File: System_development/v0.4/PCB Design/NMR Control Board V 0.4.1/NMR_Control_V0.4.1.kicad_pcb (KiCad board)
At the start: 2 copper layers, 139.7 x 88.9 mm, 57 parts

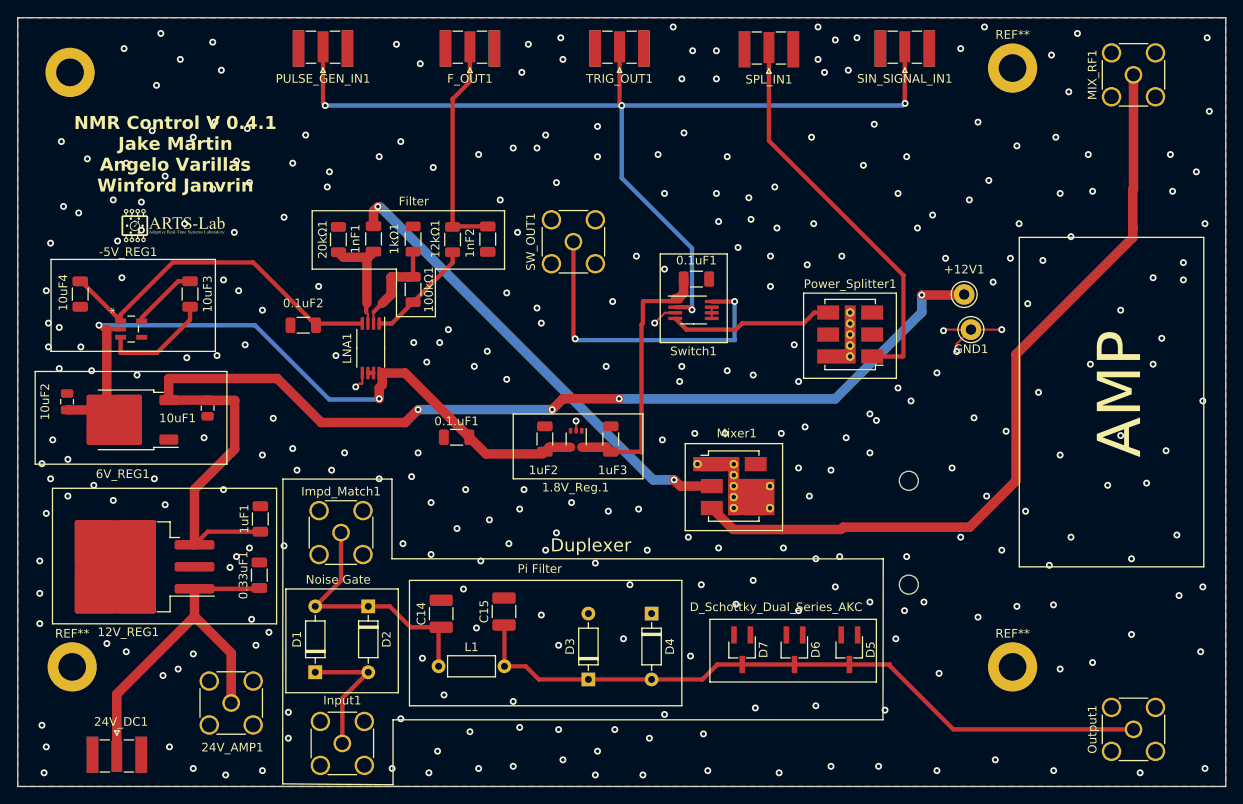
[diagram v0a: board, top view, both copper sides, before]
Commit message: Control Board 0.4.1 adjustments
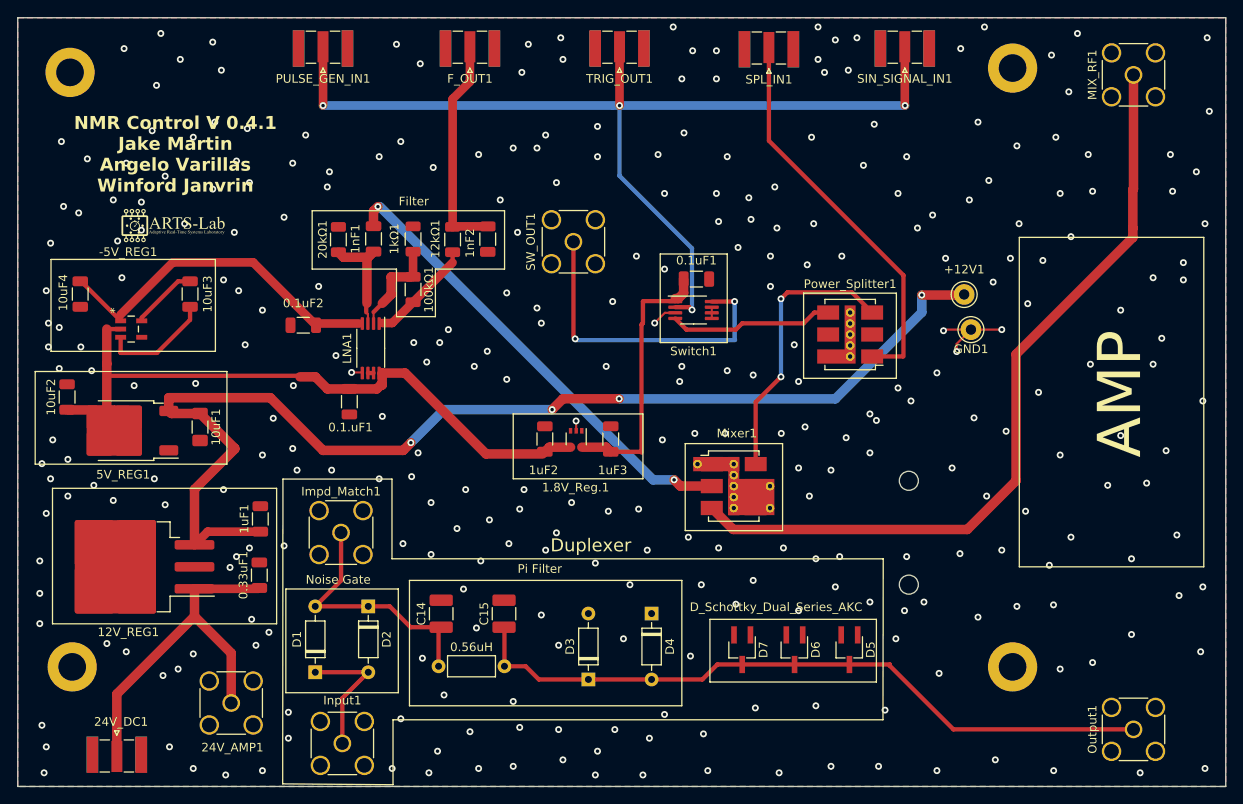
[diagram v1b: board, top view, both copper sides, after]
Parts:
- 10uF1: footprint Capacitor_SMD:C_0805_2012Metric -> Capacitor_SMD:C_1206_3216Metric_Pad1.33x1.80mm_HandSolder
- 10uF2: footprint Capacitor_SMD:C_0805_2012Metric -> Capacitor_SMD:C_1206_3216Metric
- moved 0.1.uF1 13.1 mm to (114.6, 87.6), turned to 90 degrees
- moved 10uF1 2.36 mm to (97.3, 90.5)
- moved 5V_REG1 1.25 mm to (88.6, 90.9)
- moved 10uF2 0.54 mm to (81.9, 87.0)
- moved C15 0.25 mm to (132.4, 112.1)
- renumbered L1 to 0.56uH, 6V_REG1 to 5V_REG1
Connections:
- Mixer1 pad 6: GND -> Net-(Mixer1-LO)
- Power_Splitter1 pad 3: GND -> Net-(Mixer1-LO)
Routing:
- net Net-(Mixer1-LO): track 0.00 -> 32.1 mm, vias 0 -> 2
- net Net-(-5V_REG1-V+): track 93.2 -> 86.5 mm, vias 2 -> 0
- net Net-(+12V1-In): track 138.5 -> 135.4 mm
- net GND: track 17.5 -> 16.6 mm, vias 318 -> 317
